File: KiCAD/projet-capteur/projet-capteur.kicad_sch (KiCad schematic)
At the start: 21 parts, among them J1 Power, J2 Analog, J3 Digital/PWM, J4 Digital/PWM, U2 LTC1050

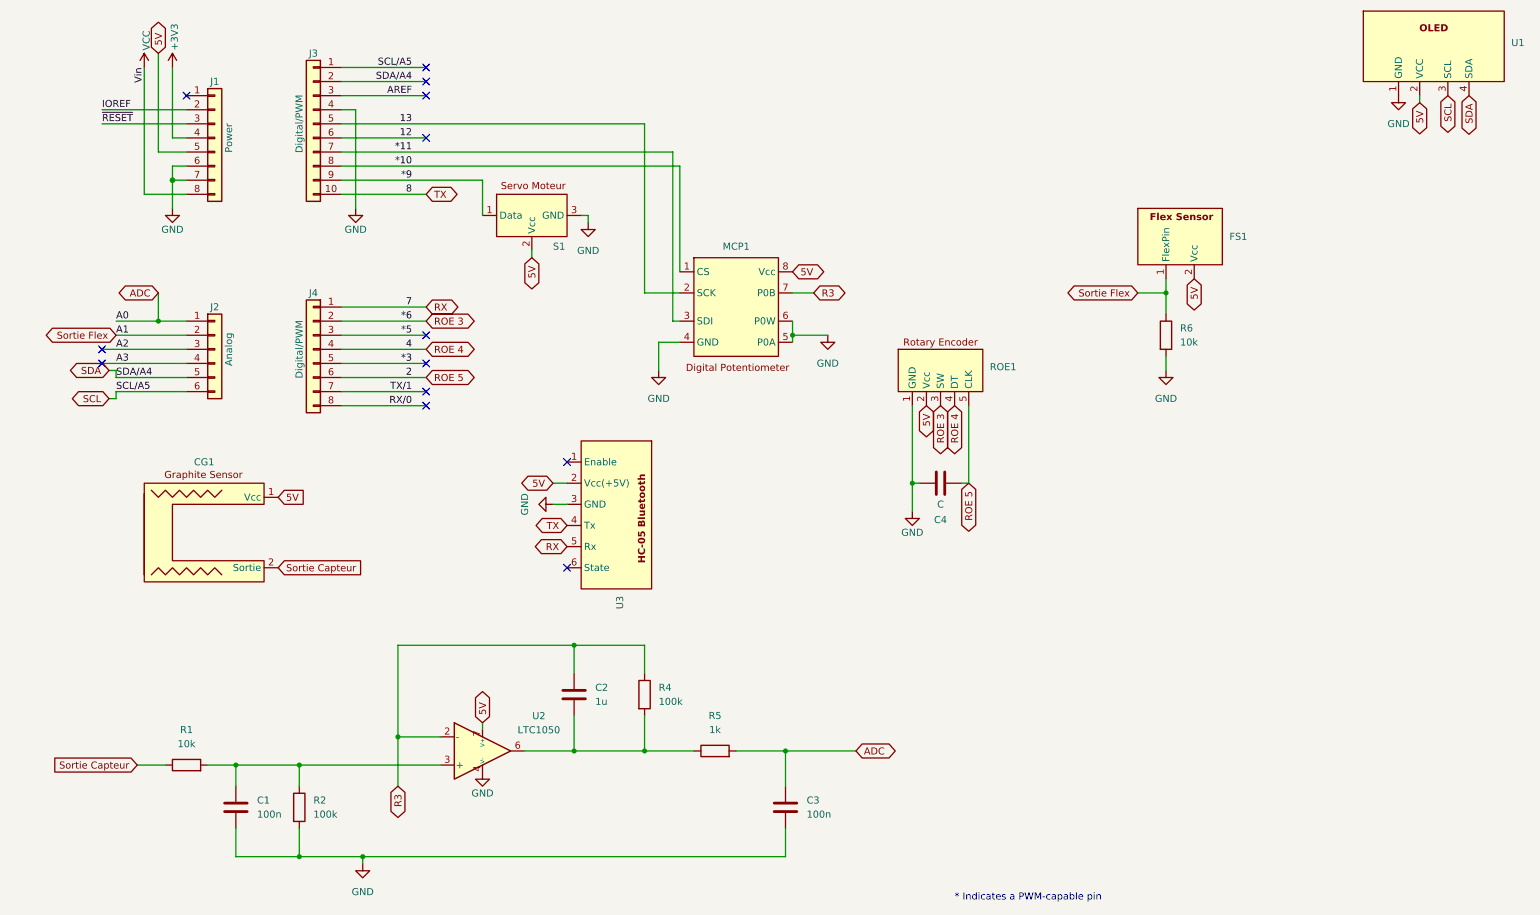
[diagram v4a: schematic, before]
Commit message: Correction du Bluetooth
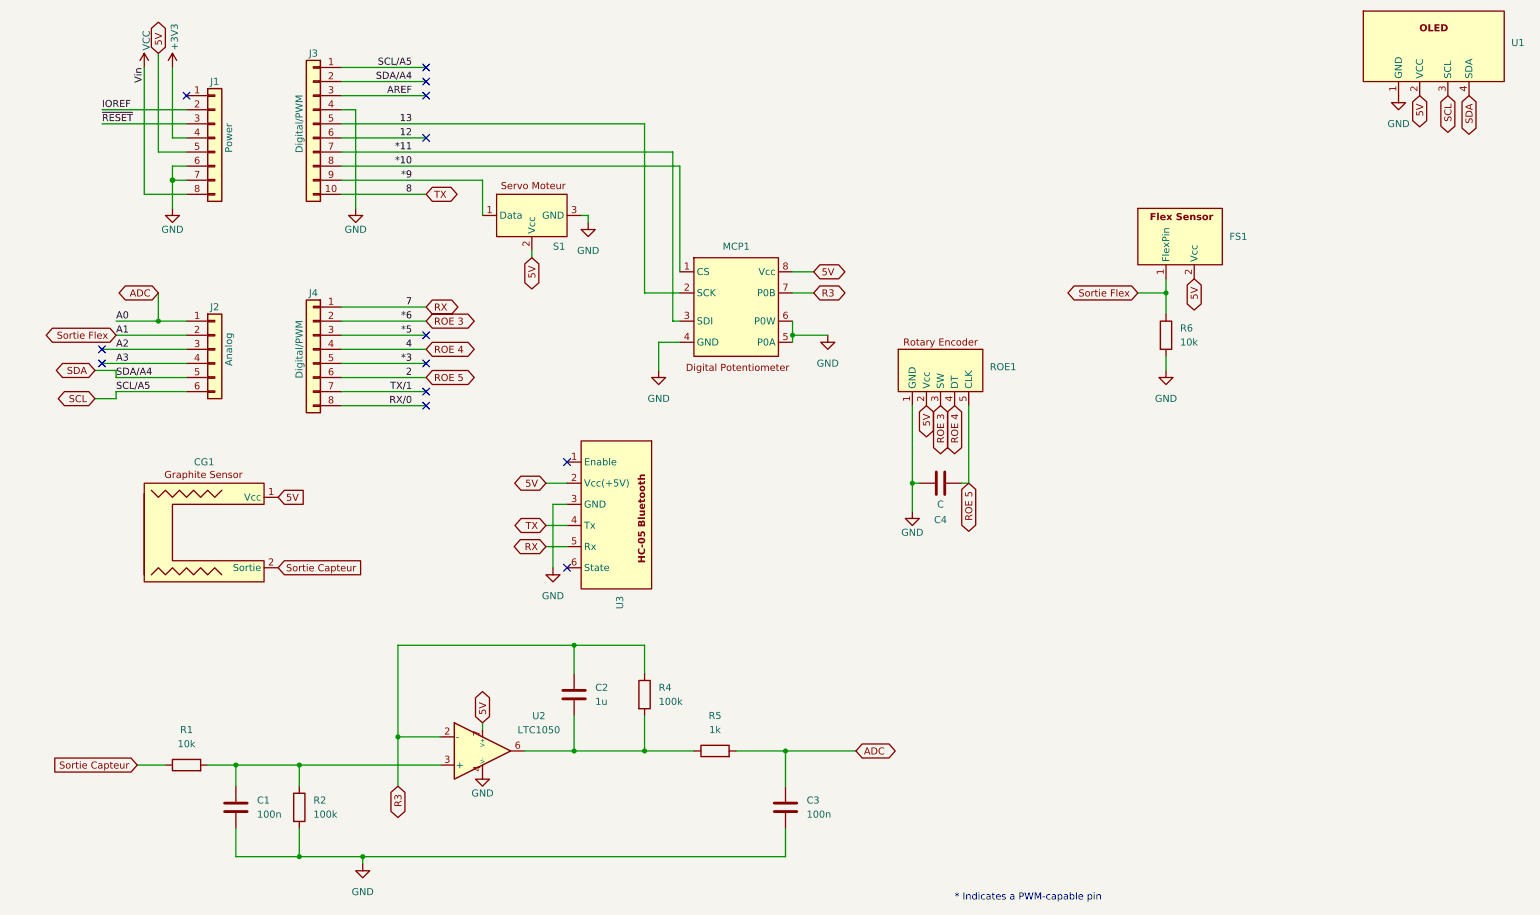
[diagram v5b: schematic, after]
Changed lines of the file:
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@@
+	(wire
+		(pts
+			(xy 104.14 102.87) (xy 107.95 102.87)
+		)
+		(stroke
+			(width 0)
+			(type default)
+		)
+	)
 	(wire
 		(pts
@@
 	(wire
 		(pts
-			(xy 107.95 102.87) (xy 105.41 102.87)
-		)
-		(stroke
-			(width 0)
-			(type default)
-		)
-	)
-	(wire
-		(pts
 			(xy 154.94 76.2) (xy 148.59 76.2)
 		)
@@
 	(wire
 		(pts
+			(xy 105.41 106.68) (xy 105.41 118.11)
+		)
+		(stroke
+			(width 0)
+			(type default)
+		)
+	)
+	(wire
+		(pts
 			(xy 26.67 87.63) (xy 26.67 86.36)
 		)
@@
 	(wire
 		(pts
+			(xy 104.14 110.49) (xy 107.95 110.49)
+		)
+		(stroke
+			(width 0)
+			(type default)
+		)
+	)
+	(wire
+		(pts
 			(xy 77.47 132.08) (xy 109.22 132.08)
 		)
@@
 	(wire
 		(pts
+			(xy 152.4 64.77) (xy 148.59 64.77)
+		)
+		(stroke
+			(width 0)
+			(type default)
+		)
+	)
+	(wire
+		(pts
 			(xy 24.13 38.1) (xy 39.37 38.1)
 		)
@@
 	(wire
 		(pts
-			(xy 261.62 34.29) (xy 261.62 33.02)
-		)
-		(stroke
-			(width 0)
-			(type default)
-		)
-	)
-	(wire
-		(pts
 			(xy 67.31 38.1) (xy 121.92 38.1)
 		)
@@
 	(wire
 		(pts
-			(xy 25.4 87.63) (xy 26.67 87.63)
+			(xy 22.86 87.63) (xy 26.67 87.63)
 		)
 		(stroke
@@
 	(wire
 		(pts
+			(xy 104.14 114.3) (xy 107.95 114.3)
+		)
+		(stroke
+			(width 0)
+			(type default)
+		)
+	)
+	(wire
+		(pts
 			(xy 77.47 148.59) (xy 77.47 132.08)
 		)
@@
 	(wire
 		(pts
-			(xy 107.95 106.68) (xy 105.41 106.68)
+			(xy 105.41 106.68) (xy 107.95 106.68)
 		)
 		(stroke
@@
 	(wire
 		(pts
-			(xy 26.67 82.55) (xy 25.4 82.55)
+			(xy 26.67 82.55) (xy 22.86 82.55)
 		)
 		(stroke
@@
 	(global_label "TX"
 		(shape bidirectional)
-		(at 107.95 110.49 180)
+		(at 104.14 110.49 180)
 		(fields_autoplaced yes)
 		(effects
@@
 		)
 		(property "Intersheetrefs" "${INTERSHEET_REFS}"
-			(at 101.6766 110.49 0)
+			(at 97.8666 110.49 0)
 			(effects
 				(font
@@
 	(global_label "RX"
 		(shape bidirectional)
-		(at 107.95 114.3 180)
+		(at 104.14 114.3 180)
 		(fields_autoplaced yes)
 		(effects
@@
 		)
 		(property "Intersheetrefs" "${INTERSHEET_REFS}"
-			(at 101.3742 114.3 0)
+			(at 97.5642 114.3 0)
 			(effects
 				(font
@@
 	(global_label "SCL"
 		(shape bidirectional)
-		(at 25.4 87.63 180)
+		(at 22.86 87.63 180)
 		(fields_autoplaced yes)
 		(effects
@@
 		)
 		(property "Intersheetrefs" "${INTERSHEET_REFS}"
-			(at 17.7961 87.63 0)
+			(at 15.2561 87.63 0)
 			(effects
 				(font
@@
 	(global_label "SDA"
 		(shape bidirectional)
-		(at 25.4 82.55 180)
+		(at 22.86 82.55 180)
 		(fields_autoplaced yes)
 		(effects
@@
 		)
 		(property "Intersheetrefs" "${INTERSHEET_REFS}"
-			(at 17.7356 82.55 0)
+			(at 15.1956 82.55 0)
 			(effects
 				(font
@@
 	(global_label "5V"
 		(shape bidirectional)
-		(at 261.62 34.29 270)
+		(at 261.62 33.02 270)
 		(fields_autoplaced yes)
 		(effects
@@
 		)
 		(property "Intersheetrefs" "${INTERSHEET_REFS}"
-			(at 261.62 40.6844 90)
+			(at 261.62 39.4144 90)
 			(effects
 				(font
@@
 	(global_label "5V"
 		(shape bidirectional)
-		(at 105.41 102.87 180)
+		(at 104.14 102.87 180)
 		(fields_autoplaced yes)
 		(effects
@@
 		)
 		(property "Intersheetrefs" "${INTERSHEET_REFS}"
-			(at 99.0156 102.87 0)
+			(at 97.7456 102.87 0)
 			(effects
 				(font
@@
 	(global_label "5V"
 		(shape bidirectional)
-		(at 148.59 64.77 0)
+		(at 152.4 64.77 0)
 		(fields_autoplaced yes)
 		(effects
@@
 		)
 		(property "Intersheetrefs" "${INTERSHEET_REFS}"
-			(at 154.9844 64.77 0)
+			(at 158.7944 64.77 0)
 			(effects
 				(font
@@
 		(lib_name "GND_2")
 		(lib_id "power:GND")
-		(at 105.41 106.68 270)
+		(at 105.41 118.11 0)
 		(unit 1)
 		(exclude_from_sim no)
@@
 		(fields_autoplaced yes)
 		(property "Reference" "#PWR1"
-			(at 99.06 106.68 0)
+			(at 105.41 124.46 0)
 			(effects
 				(font
@@
 		)
 		(property "Value" "GND"
-			(at 100.33 106.68 0)
+			(at 105.41 123.19 0)
 			(effects
 				(font
@@
 		)
 		(property "Footprint" ""
-			(at 105.41 106.68 0)
+			(at 105.41 118.11 0)
 			(effects
 				(font
@@
 		)
 		(property "Datasheet" ""
-			(at 105.41 106.68 0)
+			(at 105.41 118.11 0)
 			(effects
 				(font
@@
 		)
 		(property "Description" "Power symbol creates a global label with name \"GND\" , ground"
-			(at 105.41 106.68 0)
-			(effects
-				(font
+			(at 105.41 118.11 0)
+			(effects
+				(font

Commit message: Seance Realisation banc de test 17.03
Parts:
- C4: value C -> 100n
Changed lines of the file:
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@@
 			)
 		)
-		(property "Value" "C"
+		(property "Value" "100n"
 			(at 175.26 106.68 90)
 			(effects

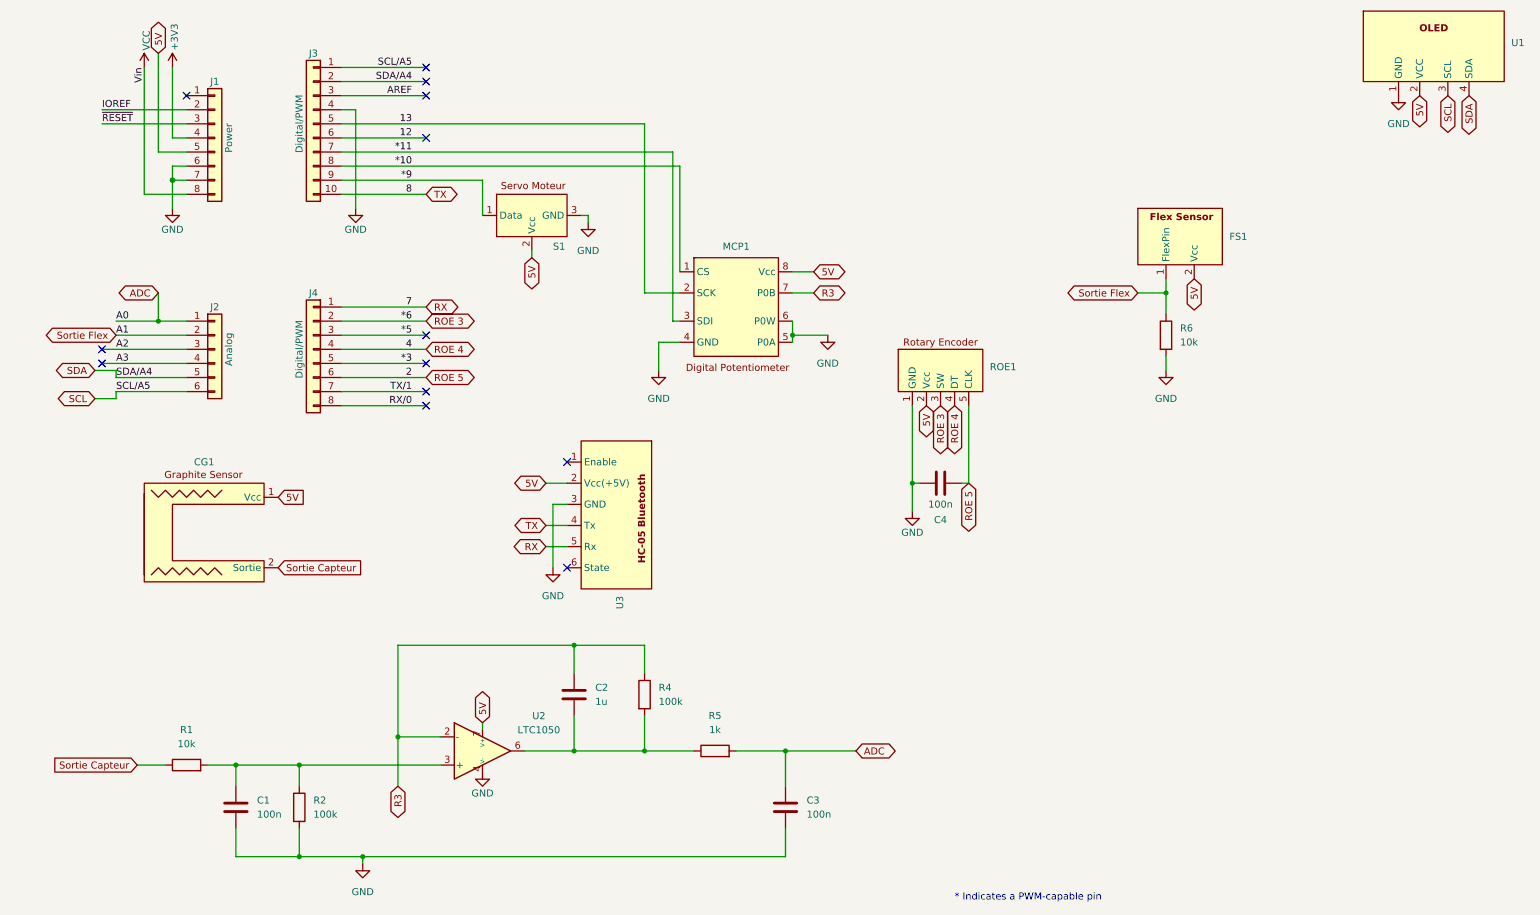
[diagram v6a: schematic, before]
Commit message: Grandissement du shield
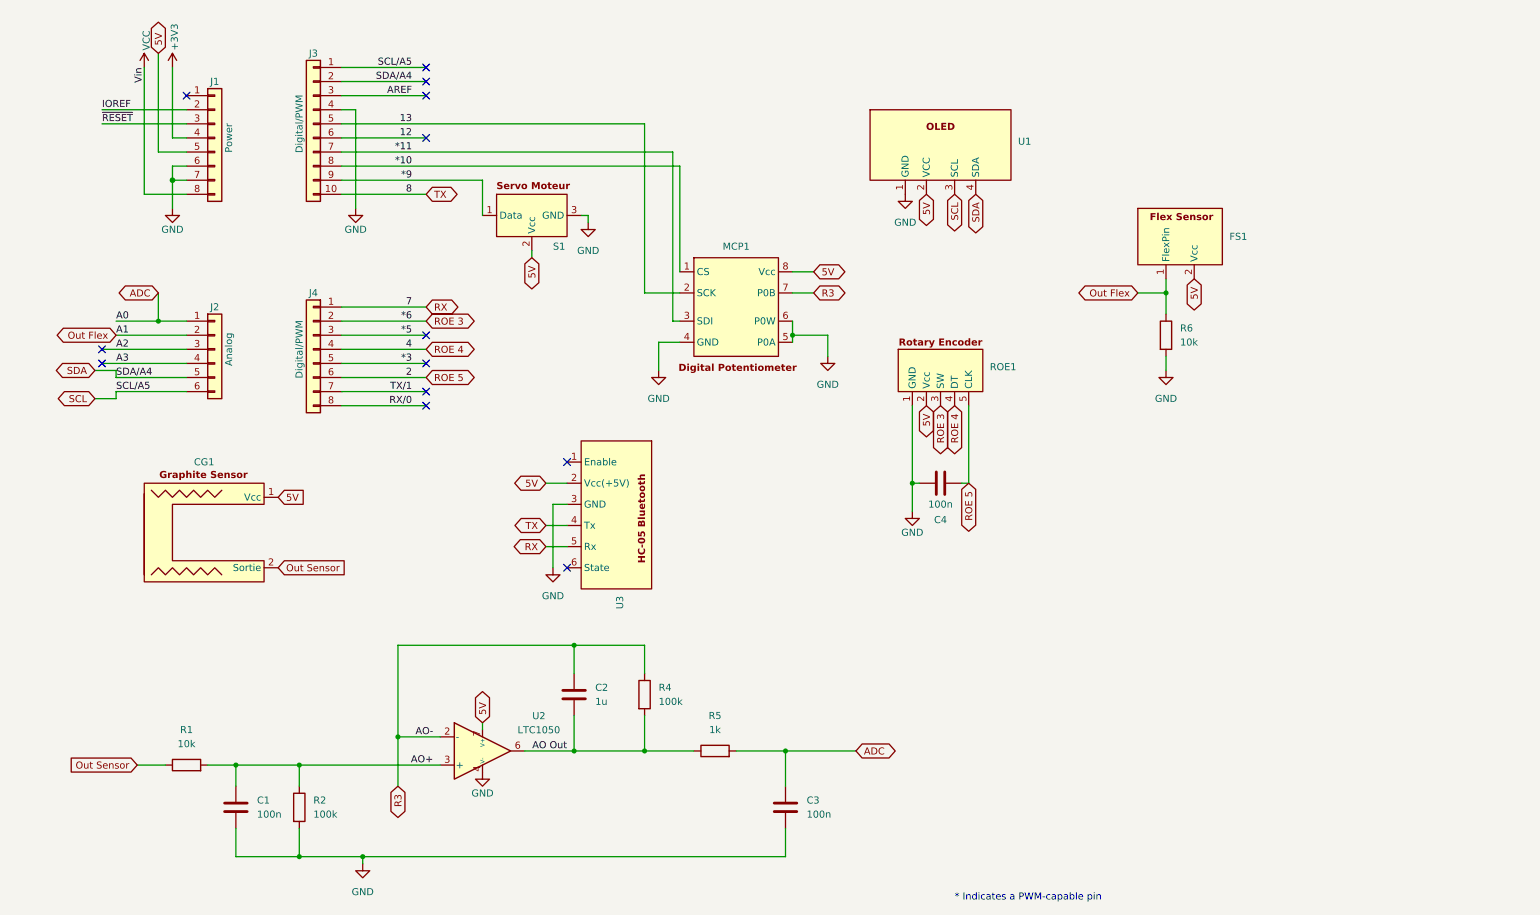
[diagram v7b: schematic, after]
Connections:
- net AO Out: now reaches C2.2, R4.2, R5.1, U2.6
- net AO+: now reaches C1.1, R1.2, R2.1, U2.3 (+)
- net Sortie Capteur renamed Out Sensor
- net Sortie Flex renamed Out Flex
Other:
- moved on the sheet: U1
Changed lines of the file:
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@@
 	)
 	(junction
-		(at 148.59 76.2)
-		(diameter 0)
-		(color 0 0 0 0)
-	)
-	(junction
 		(at 34.29 73.66)
 		(diameter 0)
@@
 	)
 	(junction
+		(at 148.59 76.2)
+		(diameter 0)
+		(color 0 0 0 0)
+	)
+	(junction
 		(at 71.12 170.18)
 		(diameter 0)
@@
 	)
 	(no_connect
-		(at 107.95 99.06)
+		(at 39.37 33.02)
 	)
 	(no_connect
-		(at 39.37 33.02)
+		(at 107.95 99.06)
 	)
 	(no_connect
@@
 	(wire
 		(pts
+			(xy 148.59 73.66) (xy 148.59 76.2)
+		)
+		(stroke
+			(width 0)
+			(type default)
+		)
+	)
+	(wire
+		(pts
 			(xy 92.71 54.61) (xy 92.71 48.26)
 		)
@@
 	(wire
 		(pts
-			(xy 154.94 76.2) (xy 148.59 76.2)
-		)
-		(stroke
-			(width 0)
-			(type default)
-		)
-	)
-	(wire
-		(pts
 			(xy 34.29 25.4) (xy 34.29 43.18)
 		)
@@
 	(wire
 		(pts
+			(xy 148.59 76.2) (xy 148.59 77.47)
+		)
+		(stroke
+			(width 0)
+			(type default)
+		)
+	)
+	(wire
+		(pts
 			(xy 152.4 64.77) (xy 148.59 64.77)
 		)
@@
 	(wire
 		(pts
-			(xy 148.59 76.2) (xy 148.59 77.47)
+			(xy 148.59 68.58) (xy 152.4 68.58)
 		)
 		(stroke
@@
 	(wire
 		(pts
-			(xy 148.59 68.58) (xy 152.4 68.58)
+			(xy 67.31 35.56) (xy 69.85 35.56)
 		)
 		(stroke
 			(width 0)
-			(type default)
+			(type solid)
 		)
 	)
 	(wire
 		(pts
-			(xy 67.31 35.56) (xy 69.85 35.56)
+			(xy 39.37 45.72) (xy 36.83 45.72)
 		)
 		(stroke
@@
 	(wire
 		(pts
-			(xy 39.37 45.72) (xy 36.83 45.72)
+			(xy 154.94 76.2) (xy 154.94 80.01)
 		)
 		(stroke
 			(width 0)
-			(type solid)
+			(type default)
 		)
 	)
@@
 	(wire
 		(pts
-			(xy 148.59 73.66) (xy 148.59 76.2)
+			(xy 43.18 153.67) (xy 48.26 153.67)
 		)
 		(stroke
@@
 	(wire
 		(pts
-			(xy 43.18 153.67) (xy 48.26 153.67)
+			(xy 148.59 76.2) (xy 154.94 76.2)
 		)
 		(stroke
@@
 		)
 	)
+	(label "AO Out"
+		(at 107.95 151.13 180)
+		(effects
+			(font
+				(size 1.27 1.27)
+			)
+			(justify right bottom)
+		)
+	)
 	(label "*11"
 		(at 80.01 43.18 180)
@@
 		)
 	)
+	(label "AO+"
+		(at 83.82 153.67 180)
+		(effects
+			(font
+				(size 1.27 1.27)
+			)
+			(justify right bottom)
+		)
+	)
 	(label "A1"
 		(at 26.67 76.2 0)
@@
 		)
 	)
+	(label "AO-"
+		(at 83.82 148.59 180)
+		(effects
+			(font
+				(size 1.27 1.27)
+			)
+			(justify right bottom)
+		)
+	)
 	(label "SDA{slash}A4"
 		(at 26.67 83.82 0)
@@
 	(global_label "SCL"
 		(shape bidirectional)
-		(at 266.7 33.02 270)
+		(at 177.8 50.8 270)
 		(fields_autoplaced yes)
 		(effects
@@
 		)
 		(property "Intersheetrefs" "${INTERSHEET_REFS}"
-			(at 266.7 40.6239 90)
+			(at 177.8 58.4039 90)
 			(effects
 				(font
@@
 		)
 	)
-	(global_label "Sortie Flex"
+	(global_label "Out Flex"
 		(shape bidirectional)
 		(at 26.67 76.2 180)
@@
 		)
 		(property "Intersheetrefs" "${INTERSHEET_REFS}"
-			(at 12.1718 76.2 0)
+			(at 14.5304 76.2 0)
 			(effects
 				(font
@@
 	(global_label "SDA"
 		(shape bidirectional)
-		(at 270.51 33.02 270)
+		(at 181.61 50.8 270)
 		(fields_autoplaced yes)
 		(effects
@@
 		)
 		(property "Intersheetrefs" "${INTERSHEET_REFS}"
-			(at 270.51 40.6844 90)
+			(at 181.61 58.4644 90)
 			(effects
 				(font
@@
 	(global_label "5V"
 		(shape bidirectional)
-		(at 261.62 33.02 270)
+		(at 172.72 50.8 270)
 		(fields_autoplaced yes)
 		(effects
@@
 		)
 		(property "Intersheetrefs" "${INTERSHEET_REFS}"
-			(at 261.62 39.4144 90)
+			(at 172.72 57.1944 90)
 			(effects
 				(font
@@
 		)
 	)
-	(global_label "Sortie Flex"
+	(global_label "Out Flex"
 		(shape bidirectional)
 		(at 210.82 68.58 180)
@@
 		)
 		(property "Intersheetrefs" "${INTERSHEET_REFS}"
-			(at 196.3218 68.58 0)
+			(at 198.6804 68.58 0)
 			(effects
 				(font
@@
 		)
 	)
-	(global_label "Sortie Capteur"
+	(global_label "Out Sensor"
 		(shape input)
 		(at 55.88 118.11 0)
@@
 		)
 		(property "Intersheetrefs" "${INTERSHEET_REFS}"
-			(at 72.8092 118.11 0)
+			(at 69.5435 118.11 0)
 			(effects
 				(font
@@
 		)
 	)
-	(global_label "Sortie Capteur"
+	(global_label "Out Sensor"
 		(shape input)
 		(at 30.48 153.67 180)
@@
 		)
 		(property "Intersheetrefs" "${INTERSHEET_REFS}"
-			(at 13.5508 153.67 0)
+			(at 16.8165 153.67 0)
 			(effects
 				(font
@@
 			)
 		)
-		(property "Datasheet" "https://www.analog.com/media/en/technical-documentation/data-sheets/1151fa.pdf"
+		(property "Datasheet" ""
 			(at 39.37 132.08 0)
 			(effects
@@
 		(lib_name "GND_2")
 		(lib_id "power:GND")
-		(at 257.81 33.02 0)
+		(at 168.91 50.8 0)
 		(unit 1)
 		(exclude_from_sim no)
@@
 		(fields_autoplaced yes)
 		(property "Reference" "#PWR02"
-			(at 257.81 39.37 0)
+			(at 168.91 57.15 0)
 			(effects
 				(font
@@
 		)
 		(property "Value" "GND"
-			(at 257.81 38.1 0)
+			(at 168.91 55.88 0)
 			(effects
 				(font
@@
 		)
 		(property "Footprint" ""
-			(at 257.81 33.02 0)
+			(at 168.91 50.8 0)
 			(effects
 				(font
@@
 		)
 		(property "Datasheet" ""
-			(at 257.81 33.02 0)
+			(at 168.91 50.8 0)
 			(effects
 				(font
@@
 		)
 		(property "Description" "Power symbol creates a global label with name \"GND\" , ground"
-			(at 257.81 33.02 0)
+			(at 168.91 50.8 0)
 			(effects
 				(font
@@
 		(lib_name "GND_2")
 		(lib_id "power:GND")
-		(at 154.94 76.2 0)
+		(at 154.94 80.01 0)
 		(unit 1)
 		(exclude_from_sim no)
@@
 		(fields_autoplaced yes)
 		(property "Reference" "#PWR07"
-			(at 154.94 82.55 0)
+			(at 154.94 86.36 0)
 			(effects
 				(font
@@
 		)
 		(property "Value" "GND"
-			(at 154.94 81.28 0)
+			(at 154.94 85.09 0)
 			(effects
 				(font
@@
 		)
 		(property "Footprint" ""
-			(at 154.94 76.2 0)
+			(at 154.94 80.01 0)
 			(effects
 				(font
@@
 		)
 		(property "Datasheet" ""
-			(at 154.94 76.2 0)
+			(at 154.94 80.01 0)
 			(effects
 				(font
@@
 		)
 		(property "Description" "Power symbol creates a global label with name \"GND\" , ground"
-			(at 154.94 76.2 0)
+			(at 154.94 80.01 0)
 			(effects
 				(font
@@
 	(symbol
 		(lib_id "MyLibGraphite:OLED")
-		(at 264.16 30.48 0)
+		(at 175.26 48.26 0)
 		(unit 1)
 		(exclude_from_sim no)
@@
 		(fields_autoplaced yes)
 		(property "Reference" "U1"
-			(at 278.13 23.4949 0)
+			(at 189.23 41.2749 0)
 			(effects
 				(font
@@
 		)
 		(property "Value" "~"
-			(at 278.13 25.4 0)
+			(at 189.23 43.18 0)
 			(effects
 				(font
@@
 		)
 		(property "Footprint" "MyLibEmpreinte:MyEmpreinte"
-			(at 264.16 30.48 0)
+			(at 175.26 48.26 0)
 			(effects
 				(font
@@
 		)
 		(property "Datasheet" ""
-			(at 264.16 30.48 0)
+			(at 175.26 48.26 0)
 			(effects
 				(font
@@
 		)
 		(property "Description" ""
-			(at 264.16 30.48 0)
+			(at 175.26 48.26 0)
 			(effects
 				(font
